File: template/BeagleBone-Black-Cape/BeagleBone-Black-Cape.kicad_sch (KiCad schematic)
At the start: 2 parts, among them P8 BeagleBone_Black_Header, P9 BeagleBone_Black_Header

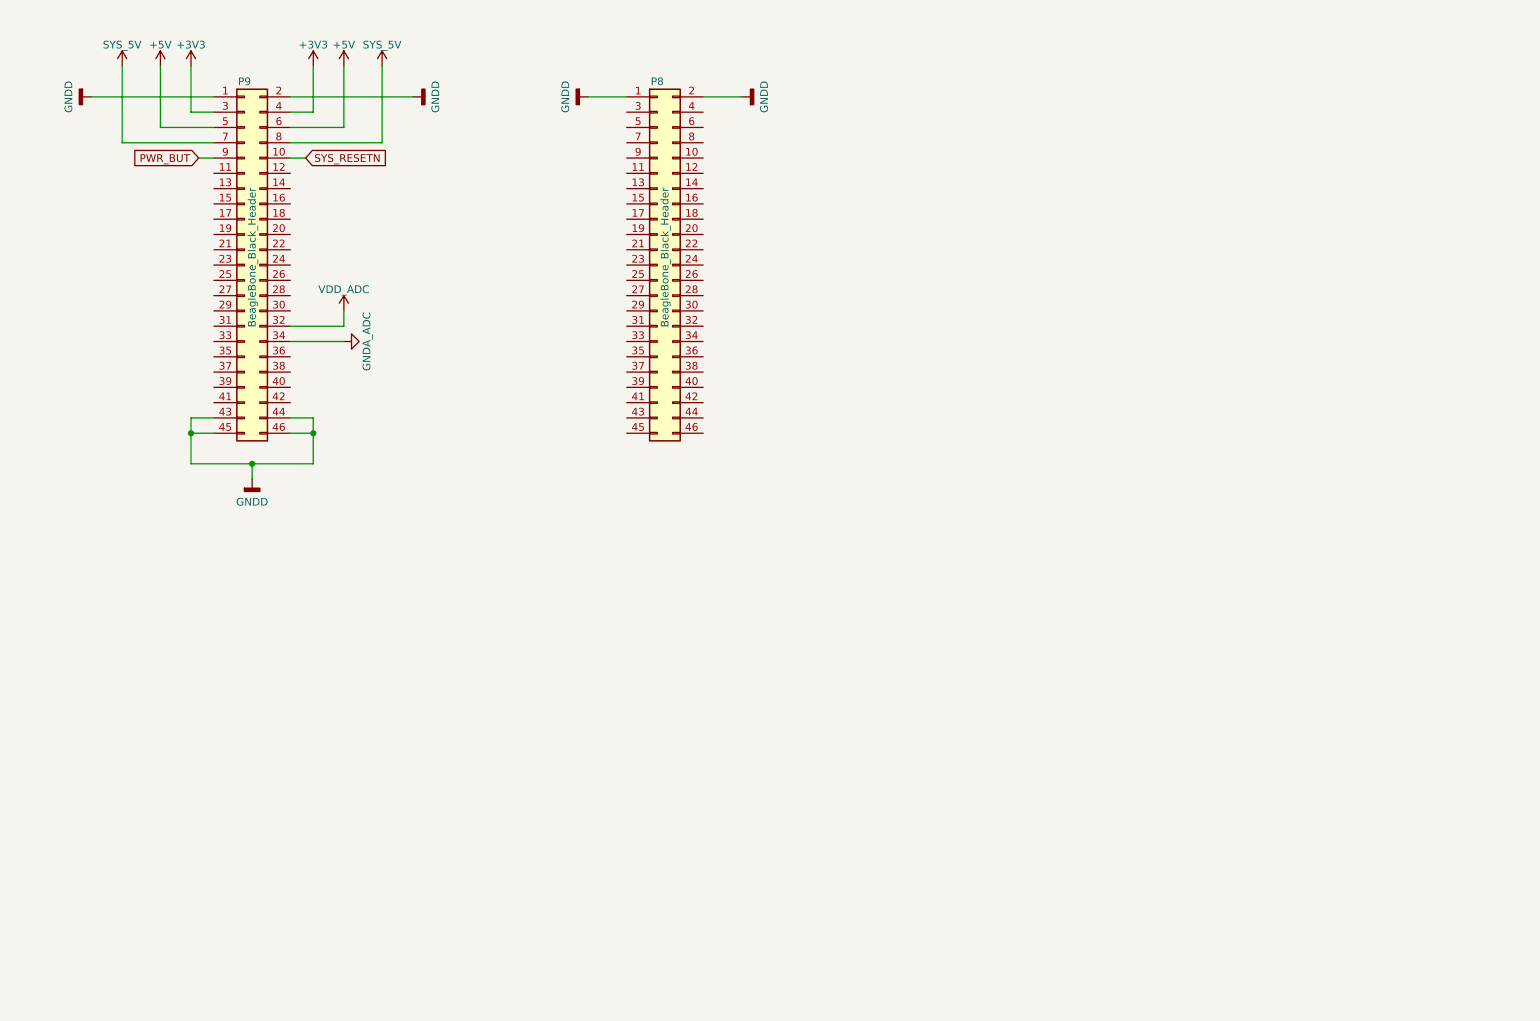
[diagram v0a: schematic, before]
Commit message: fix: change original libs; add: new components
- Fix LIS3DH pins positions;
- Add ATmega164P symbol;
- Add 3D model to the L_Wuerth_HCM-7050;
- Add parameters for R_RES (Assembly...).
- Add parameters for R_RES and C_CAP;
- Fix SOIC-8 package 3D model;
- Add new parameters for many symbols;
- Change text height from 70 mil to 50 mil;
- Add solder mask expansion for 2-contact jumpers;
- Change thermopad vias of QFN-20-1EP_3x3mm_P0.45mm_EP1.6x1.6mm_ThermalVias;
- Add D_SMAF footprint;
- Fillet silk for C_1206;
-Rectangle silk for R_1206;
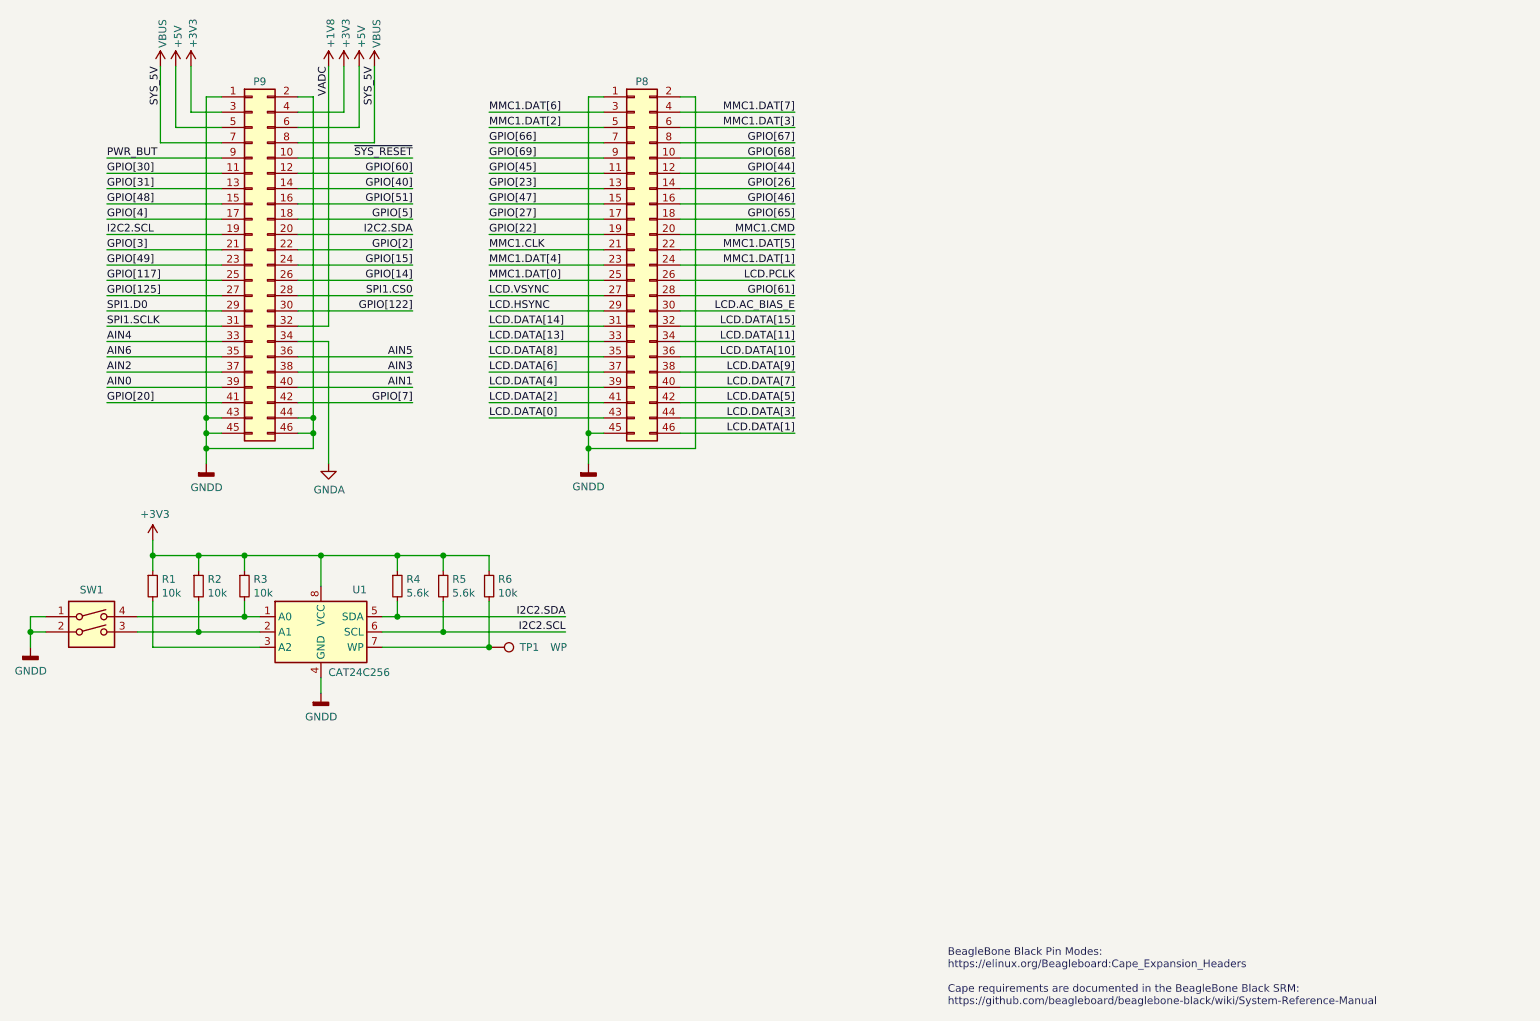
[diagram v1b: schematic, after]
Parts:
- added R1, R2, R3, R6: 10k, symbol Device:R_Small
- added R4, R5: 5.6k, symbol Device:R_Small
- added SW1: SW_DIP_x02, symbol Switch:SW_DIP_x02
- added TP1: WP, symbol Connector:TestPoint
- added U1: CAT24C256, symbol Memory_EEPROM:CAT24C256
- P8, P9: footprint Socket_BeagleBone_Black:Socket_BeagleBone_Black -> Connector_PinHeader_2.54mm:PinHeader_2x23_P2.54mm_Vertical
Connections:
- net +3V3: now also R1.1, R2.1, R3.1, R4.1, R5.1, R6.1, U1.8 (VCC)
- net GNDD: now also P8.45 (Pin_45), SW1.1, SW1.2, U1.4 (GND)
- net GPIO[30]: now reaches P9.11 (Pin_11)
- net GPIO[60]: now reaches P9.12 (Pin_12)
- net GPIO[31]: now reaches P9.13 (Pin_13)
- net GPIO[40]: now reaches P9.14 (Pin_14)
- net GPIO[48]: now reaches P9.15 (Pin_15)
- net GPIO[51]: now reaches P9.16 (Pin_16)
- net GPIO[4]: now reaches P9.17 (Pin_17)
- net GPIO[5]: now reaches P9.18 (Pin_18)
- net I2C2.SCL: now reaches P9.19 (Pin_19)
- net I2C2.SCL: now also R5.2, U1.6 (SCL)
- net I2C2.SDA: now reaches P9.20 (Pin_20)
- net I2C2.SDA: now also R4.2, U1.5 (SDA)
- net GPIO[3]: now reaches P9.21 (Pin_21)
- net GPIO[2]: now reaches P9.22 (Pin_22)
- net GPIO[49]: now reaches P9.23 (Pin_23)
- net GPIO[15]: now reaches P9.24 (Pin_24)
- net GPIO[117]: now reaches P9.25 (Pin_25)
- net GPIO[14]: now reaches P9.26 (Pin_26)
- net GPIO[125]: now reaches P9.27 (Pin_27)
- net SPI1.CS0: now reaches P9.28 (Pin_28)
- net SPI1.D0: now reaches P9.29 (Pin_29)
- net GPIO[122]: now reaches P9.30 (Pin_30)
- net SPI1.SCLK: now reaches P9.31 (Pin_31)
- net AIN4: now reaches P9.33 (Pin_33)
- net AIN6: now reaches P9.35 (Pin_35)
- net AIN5: now reaches P9.36 (Pin_36)
- net AIN2: now reaches P9.37 (Pin_37)
- net AIN3: now reaches P9.38 (Pin_38)
- net AIN0: now reaches P9.39 (Pin_39)
- net AIN1: now reaches P9.40 (Pin_40)
- net GPIO[20]: now reaches P9.41 (Pin_41)
- net GPIO[7]: now reaches P9.42 (Pin_42)
- net GPIO[68]: now reaches P8.10 (Pin_10)
- net GPIO[45]: now reaches P8.11 (Pin_11)
- net GPIO[44]: now reaches P8.12 (Pin_12)
- net GPIO[23]: now reaches P8.13 (Pin_13)
- net GPIO[26]: now reaches P8.14 (Pin_14)
- net GPIO[47]: now reaches P8.15 (Pin_15)
- net GPIO[46]: now reaches P8.16 (Pin_16)
- net GPIO[27]: now reaches P8.17 (Pin_17)
- net GPIO[65]: now reaches P8.18 (Pin_18)
- net GPIO[22]: now reaches P8.19 (Pin_19)
- net MMC1.CMD: now reaches P8.20 (Pin_20)
- net MMC1.CLK: now reaches P8.21 (Pin_21)
- net MMC1.DAT[5]: now reaches P8.22 (Pin_22)
- net MMC1.DAT[4]: now reaches P8.23 (Pin_23)
- net MMC1.DAT[1]: now reaches P8.24 (Pin_24)
- net MMC1.DAT[0]: now reaches P8.25 (Pin_25)
- net LCD.PCLK: now reaches P8.26 (Pin_26)
- net LCD.VSYNC: now reaches P8.27 (Pin_27)
- net GPIO[61]: now reaches P8.28 (Pin_28)
- net LCD.HSYNC: now reaches P8.29 (Pin_29)
- net MMC1.DAT[6]: now reaches P8.3 (Pin_3)
- net LCD.AC_BIAS_E: now reaches P8.30 (Pin_30)
- net LCD.DATA[14]: now reaches P8.31 (Pin_31)
- net LCD.DATA[15]: now reaches P8.32 (Pin_32)
- net LCD.DATA[13]: now reaches P8.33 (Pin_33)
- net LCD.DATA[11]: now reaches P8.34 (Pin_34)
- net LCD.DATA[8]: now reaches P8.35 (Pin_35)
- net LCD.DATA[10]: now reaches P8.36 (Pin_36)
- net LCD.DATA[6]: now reaches P8.37 (Pin_37)
- net LCD.DATA[9]: now reaches P8.38 (Pin_38)
- net LCD.DATA[4]: now reaches P8.39 (Pin_39)
- net MMC1.DAT[7]: now reaches P8.4 (Pin_4)
- net LCD.DATA[7]: now reaches P8.40 (Pin_40)
- net LCD.DATA[2]: now reaches P8.41 (Pin_41)
- net LCD.DATA[5]: now reaches P8.42 (Pin_42)
- net LCD.DATA[0]: now reaches P8.43 (Pin_43)
- net LCD.DATA[3]: now reaches P8.44 (Pin_44)
- net LCD.DATA[1]: now reaches P8.46 (Pin_46)
- net MMC1.DAT[2]: now reaches P8.5 (Pin_5)
- net MMC1.DAT[3]: now reaches P8.6 (Pin_6)
- net GPIO[66]: now reaches P8.7 (Pin_7)
- net GPIO[67]: now reaches P8.8 (Pin_8)
- net GPIO[69]: now reaches P8.9 (Pin_9)
- net GNDA_ADC renamed GNDA
- net SYS_5V renamed VBUS
- net SYS_RESETN renamed ~{SYS_RESET}
- net VDD_ADC renamed +1V8
- new net: R6.2, TP1.1, U1.7 (WP)
- new net: R1.2, U1.3 (A2)
- new net: R3.2, SW1.4, U1.1 (A0)
- new net: R2.2, SW1.3, U1.2 (A1)
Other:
- note added: "BeagleBone Black Pin Modes: https://elinux.org/Beagleboard:Cape_Expansion_Headers Cape requirements are documented in the BeagleBone Black SRM: https://github.com/beagleboard/beaglebone-black/wiki/System-Reference-Manual"
- moved on the sheet: P8, P9
